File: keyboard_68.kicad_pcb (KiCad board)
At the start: 2 copper layers, 330.2 x 92.3 mm, 305 parts, among them J1 Conn_01x02_Male, J10 Conn_01x02_Female, J11 Conn_01x02_Female, J12 Conn_01x02_Female, J13 Conn_01x02_Female, J14 Conn_01x02_Female, J15 Conn_01x02_Female, J16 Conn_01x02_Female, J17 Conn_01x02_Female, J18 Conn_01x02_Female, J19 Conn_01x02_Female, J2 Conn_01x02_Female, J20 Conn_01x02_Female, J21 Conn_01x02_Female, J22 Conn_01x02_Female, J23 Conn_01x02_Female, J24 Conn_01x02_Female, J25 Conn_01x02_Female, J26 Conn_01x02_Female, J27 Conn_01x02_Female, J28 Conn_01x02_Female, J29 Conn_01x02_Female, J3 Conn_01x02_Female, J30 Conn_01x02_Female, J31 Conn_01x02_Female, J32 Conn_01x02_Female, J33 Conn_01x02_Female, J34 Conn_01x02_Female, J35 Conn_01x02_Female, J36 Conn_01x02_Female, J37 Conn_01x02_Female, J38 Conn_01x02_Female, J39 Conn_01x02_Female, J4 Conn_01x02_Female, J40 Conn_01x02_Female, J41 Conn_01x02_Female, J42 Conn_01x02_Female, J43 Conn_01x02_Female, J44 Conn_01x02_Female, J45 Conn_01x02_Female, J46 Conn_01x02_Female, J47 Conn_01x02_Female, J48 Conn_01x02_Female, J49 Conn_01x02_Female, J5 Conn_01x02_Female, J50 Conn_01x02_Female, J51 Conn_01x02_Female, J52 Conn_01x02_Female, J53 Conn_01x02_Female, J54 Conn_01x02_Female, J55 Conn_01x02_Female, J56 Conn_01x02_Female, J57 Conn_01x02_Female, J58 Conn_01x02_Female, J59 Conn_01x02_Female, J6 Conn_01x02_Female, J60 Conn_01x02_Female, J61 Conn_01x02_Female, J62 Conn_01x02_Female, J63 Conn_01x02_Female, J64 Conn_01x02_Female, J65 Conn_01x02_Female, J66 Conn_01x02_Female, J67 Conn_01x02_Female, J68 Conn_01x02_Female, J69 Conn_01x02_Female, J7 Conn_01x02_Female, J8 Conn_01x02_Female, J9 Conn_01x02_Female, Q1 DMG2305, U1 USB_C, U2 nRF52840_som, U3 MT3608

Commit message: V2
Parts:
- removed RESET: SW_Push, Button_Switch_SMD:Panasonic_EVQPUJ_EVQPUA
- added J70: Conn_02x03_Odd_Even, Connector:Tag-Connect_TC2030-IDC-NL_2x03_P1.27mm_Vertical, B.Cu at (360.2, 86.4)
- added R10: 100k, Resistor_SMD:R_0805_2012Metric, F.Cu at (346.5, 68.3)
- added R9: 100k, Resistor_SMD:R_0805_2012Metric, F.Cu at (346.5, 70.4)
- added SW1: SW_Push, Button_Switch_SMD:Panasonic_EVQPUJ_EVQPUA, F.Cu at (369.8, 87.4)
- C73, D11, D16, D26, D4, D5, D59, D6, D62, D9, FB1, FB2, L1, R2, R3, R4, R7, U3: moved to B.Cu
- U1: footprint USB_C_Receptacle_Amphenol_12401610E4-2A:USB_C_Receptacle_Amphenol_12401610E4-2A -> Connector_USB:USB_C_Receptacle_Amphenol_12401610E4-2A
- moved FB2 5.31 mm to (326.0, 38.2)
- moved FB1 4.14 mm to (327.3, 38.2)
- moved R2 3.95 mm to (322.3, 36.6), turned to 180 degrees
- moved C3 1.81 mm to (136.5, 74.3)
- moved C18 1.68 mm to (156.2, 74.3)
- moved C39 1.65 mm to (236.5, 36.4)
- moved C62 1.65 mm to (179.2, 36.4)
- moved C43 1.61 mm to (80.0, 74.3)
- moved C34 1.61 mm to (203.3, 112.4)
- moved C10 1.55 mm to (73.2, 112.4)
- moved C16 1.55 mm to (127.7, 112.4)
- moved C25 1.55 mm to (167.8, 112.4)
- moved C44 1.55 mm to (251.3, 74.3)
- moved C46 1.55 mm to (99.3, 74.3)
- moved C56 1.55 mm to (300.9, 74.3)
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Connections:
- net Net-(C2-Pad2) renamed nRST
- U2 pad 10: COLUMN_9 -> Net-(U2-Pad10)
- U2 pad 11: COLUMN_8 -> Net-(U2-Pad11)
- U2 pad 12: COLUMN_7 -> Net-(U2-Pad12)
- U2 pad 13: COLUMN_6 -> COLUMN_5
- U2 pad 14: COLUMN_5 -> Net-(U2-Pad14)
- U2 pad 17: COLUMN_2 -> Net-(U2-Pad17)
- U2 pad 18: Net-(U2-Pad18) -> COLUMN_0
- U2 pad 19: Net-(U2-Pad19) -> COLUMN_1
- U2 pad 20: COLUMN_1 -> COLUMN_2
- U2 pad 21: COLUMN_0 -> Net-(U2-Pad21)
- U2 pad 24: Net-(U2-Pad24) -> COLUMN_14
- U2 pad 26: Net-(U2-Pad26) -> ROW_2
- U2 pad 28: Net-(U2-Pad28) -> COLUMN_6
- U2 pad 3: COLUMN_15 -> Net-(U2-Pad3)
- U2 pad 34: Net-(U2-Pad34) -> COLUMN_13
- U2 pad 36: Net-(U2-Pad36) -> COLUMN_12
- U2 pad 38: Net-(U2-Pad38) -> VDIV
- U2 pad 4: COLUMN_14 -> ROW_0
- U2 pad 40: LED_DATA -> COLUMN_10
- U2 pad 42: Net-(U2-Pad42) -> LED_DATA
- U2 pad 45: Net-(U2-Pad45) -> ROW_3
- U2 pad 46: Net-(U2-Pad46) -> COLUMN_11
- U2 pad 49: Net-(U2-Pad49) -> COLUMN_7
- U2 pad 5: COLUMN_13 -> Net-(U2-Pad5)
- U2 pad 50: ROW_0 -> Net-(U2-Pad50)
- U2 pad 51: ROW_1 -> COLUMN_8
- U2 pad 52: ROW_2 -> Net-(U2-Pad52)
- U2 pad 53: ROW_3 -> COLUMN_9
- U2 pad 54: ROW_4 -> Net-(U2-Pad54)
- U2 pad 56: Net-(U2-Pad56) -> SWCLK
- U2 pad 57: Net-(U2-Pad57) -> SWDIO
- U2 pad 58: Net-(U2-Pad58) -> ROW_4
- U2 pad 6: COLUMN_12 -> ROW_1
- U2 pad 7: COLUMN_11 -> Net-(U2-Pad7)
- U2 pad 8: COLUMN_10 -> COLUMN_15
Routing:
- net COLUMN_5: track 290.3 -> 403.3 mm, vias 5 -> 7
- net GND: track 307.4 -> 217.0 mm, vias 154 -> 149
- net COLUMN_6: track 273.3 -> 348.7 mm
- net COLUMN_4: track 312.6 -> 383.1 mm, vias 3 -> 6
- net COLUMN_10: track 208.6 -> 161.8 mm
- net LED_POWER: track 95.1 -> 48.7 mm, vias 48 -> 10
- net COLUMN_12: track 136.3 -> 94.9 mm, vias 1 -> 4
- net COLUMN_11: track 187.9 -> 148.9 mm, vias 1 -> 2
- net COLUMN_14: track 63.5 -> 25.0 mm, vias 3 -> 1
- net ROW_0: track 398.3 -> 363.8 mm, vias 2 -> 0
- net ROW_2: track 328.6 -> 295.9 mm, vias 0 -> 2
- net COLUMN_13: track 91.6 -> 64.7 mm
- net ROW_1: track 365.7 -> 339.5 mm, vias 2 -> 0
- net COLUMN_9: track 231.7 -> 207.5 mm, vias 5 -> 3
- net COLUMN_8: track 244.8 -> 220.8 mm, vias 5 -> 3
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- removed copper zone on F.Cu, net Net-(C1-Pad1)
- removed copper zone on F.Cu, net VDD_BAT
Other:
- board size 330.2 x 92.3 mm -> 330 x 94 mm
- net class LED_POWER: clearance 0.2 -> 0.3; trace_width 0.6 -> 0.5
- net class VBAT added: clearance 0.3, trace_width 0.5, via_dia 0.6, via_drill 0.4
- net class VBUS: clearance 0.2 -> 0.3; trace_width 0.6 -> 0.5
- board text added: "Keyboard_68 Rev.: 2.0 (c) crohloff"

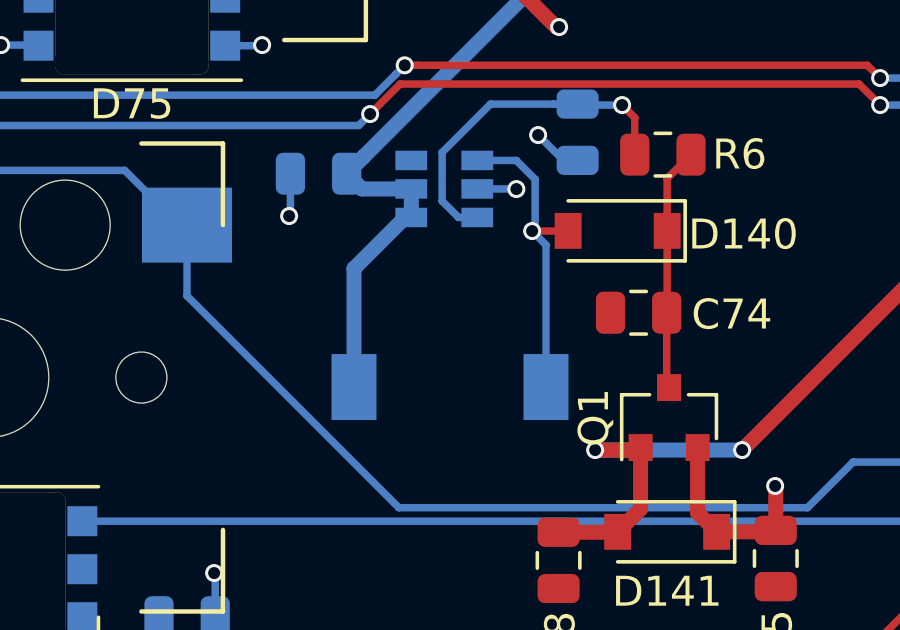
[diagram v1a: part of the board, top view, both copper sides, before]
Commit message: changed inductor and usb connector
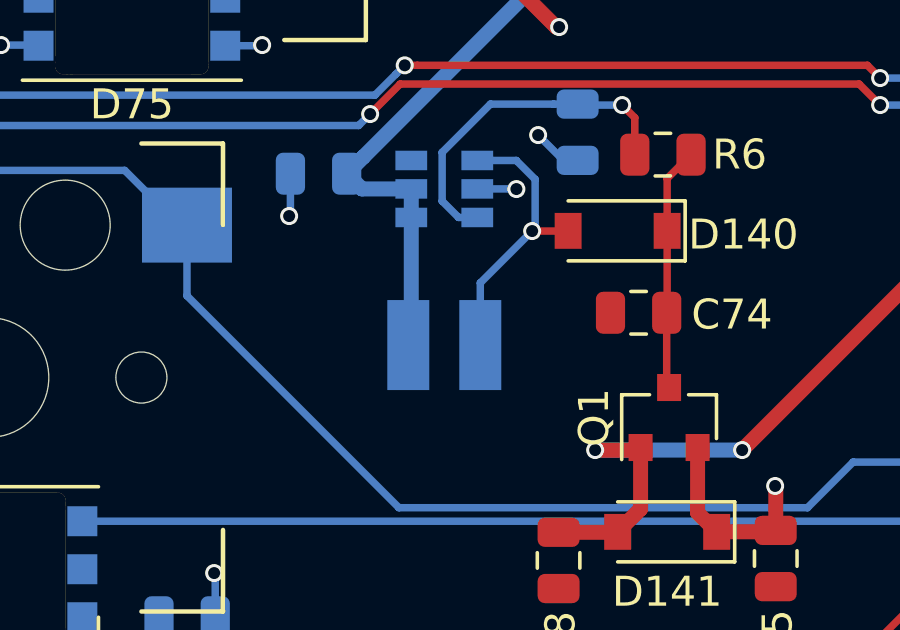
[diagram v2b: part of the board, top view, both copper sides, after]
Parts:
- L1: footprint Inductor_SMD:L_7.3x7.3_H4.5 -> L_3x3_H1.5:L_3x3_H1.5
- U1: footprint Connector_USB:USB_C_Receptacle_Amphenol_12401610E4-2A -> USB_C_Receptacle_Amphenol_12401610E4-2A:USB_C_Receptacle_Amphenol_12401610E4-2A
- moved L1 1.41 mm to (318.1, 87.5)
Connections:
- D127 pad 2: Net-(D127-Pad2) -> (no net)
- J70 pad 6: Net-(J70-Pad6) -> (no net)
- U1 pad A10: Net-(U1-PadA10) -> (no net)
- U1 pad A11: Net-(U1-PadA11) -> (no net)
- U1 pad A2: Net-(U1-PadA2) -> (no net)
- U1 pad A3: Net-(U1-PadA3) -> (no net)
- U1 pad A8: Net-(U1-PadA8) -> (no net)
- U1 pad B10: Net-(U1-PadB10) -> (no net)
- U1 pad B11: Net-(U1-PadB11) -> (no net)
- U1 pad B2: Net-(U1-PadB2) -> (no net)
- U1 pad B3: Net-(U1-PadB3) -> (no net)
- U1 pad B8: Net-(U1-PadB8) -> (no net)
- U2 pad 10: Net-(U2-Pad10) -> (no net)
- U2 pad 11: Net-(U2-Pad11) -> (no net)
- U2 pad 12: Net-(U2-Pad12) -> (no net)
- U2 pad 14: Net-(U2-Pad14) -> (no net)
- U2 pad 17: Net-(U2-Pad17) -> (no net)
- U2 pad 2: Net-(U2-Pad2) -> (no net)
- U2 pad 21: Net-(U2-Pad21) -> (no net)
- U2 pad 23: Net-(U2-Pad23) -> (no net)
- U2 pad 25: Net-(U2-Pad25) -> (no net)
- U2 pad 27: Net-(U2-Pad27) -> (no net)
- U2 pad 3: Net-(U2-Pad3) -> (no net)
- U2 pad 35: Net-(U2-Pad35) -> (no net)
- U2 pad 37: Net-(U2-Pad37) -> (no net)
- U2 pad 41: Net-(U2-Pad41) -> (no net)
- U2 pad 43: Net-(U2-Pad43) -> (no net)
- U2 pad 44: Net-(U2-Pad44) -> (no net)
- U2 pad 47: Net-(U2-Pad47) -> (no net)
- U2 pad 48: Net-(U2-Pad48) -> (no net)
- U2 pad 5: Net-(U2-Pad5) -> (no net)
- U2 pad 50: Net-(U2-Pad50) -> (no net)
- U2 pad 52: Net-(U2-Pad52) -> (no net)
- U2 pad 54: Net-(U2-Pad54) -> (no net)
- U2 pad 7: Net-(U2-Pad7) -> (no net)
- U2 pad 9: Net-(U2-Pad9) -> (no net)
- U3 pad 6: Net-(U3-Pad6) -> (no net)
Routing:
- net VDD_BAT: track 47.4 -> 45.3 mm
- net Net-(D140-Pad2): track 10.5 -> 9.67 mm

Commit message: reset switch model added
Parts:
- SW1: footprint Button_Switch_SMD:Panasonic_EVQPUJ_EVQPUA -> custom_footprints:Panasonic_EVQPUJ_EVQPUA
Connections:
- D127 pad 2: (no net) -> Net-(D127-Pad2)
- J70 pad 6: (no net) -> Net-(J70-Pad6)
- U1 pad A10: (no net) -> Net-(U1-PadA10)
- U1 pad A11: (no net) -> Net-(U1-PadA11)
- U1 pad A2: (no net) -> Net-(U1-PadA2)
- U1 pad A3: (no net) -> Net-(U1-PadA3)
- U1 pad A8: (no net) -> Net-(U1-PadA8)
- U1 pad B10: (no net) -> Net-(U1-PadB10)
- U1 pad B11: (no net) -> Net-(U1-PadB11)
- U1 pad B2: (no net) -> Net-(U1-PadB2)
- U1 pad B3: (no net) -> Net-(U1-PadB3)
- U1 pad B8: (no net) -> Net-(U1-PadB8)
- U2 pad 10: (no net) -> Net-(U2-Pad10)
- U2 pad 11: (no net) -> Net-(U2-Pad11)
- U2 pad 12: (no net) -> Net-(U2-Pad12)
- U2 pad 14: (no net) -> Net-(U2-Pad14)
- U2 pad 17: (no net) -> Net-(U2-Pad17)
- U2 pad 2: (no net) -> Net-(U2-Pad2)
- U2 pad 21: (no net) -> Net-(U2-Pad21)
- U2 pad 23: (no net) -> Net-(U2-Pad23)
- U2 pad 25: (no net) -> Net-(U2-Pad25)
- U2 pad 27: (no net) -> Net-(U2-Pad27)
- U2 pad 3: (no net) -> Net-(U2-Pad3)
- U2 pad 35: (no net) -> Net-(U2-Pad35)
- U2 pad 37: (no net) -> Net-(U2-Pad37)
- U2 pad 41: (no net) -> Net-(U2-Pad41)
- U2 pad 43: (no net) -> Net-(U2-Pad43)
- U2 pad 44: (no net) -> Net-(U2-Pad44)
- U2 pad 47: (no net) -> Net-(U2-Pad47)
- U2 pad 48: (no net) -> Net-(U2-Pad48)
- U2 pad 5: (no net) -> Net-(U2-Pad5)
- U2 pad 50: (no net) -> Net-(U2-Pad50)
- U2 pad 52: (no net) -> Net-(U2-Pad52)
- U2 pad 54: (no net) -> Net-(U2-Pad54)
- U2 pad 7: (no net) -> Net-(U2-Pad7)
- U2 pad 9: (no net) -> Net-(U2-Pad9)
- U3 pad 6: (no net) -> Net-(U3-Pad6)

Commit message: pulled usb connector out
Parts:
- moved U1 12.0 mm to (326.8, 16.4)
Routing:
- net Net-(D1-Pad2): track 26.3 -> 39.2 mm
- net Net-(R1-Pad1): track 11.2 -> 23.2 mm
- net Net-(R2-Pad1): track 12.2 -> 24.2 mm
- net Net-(C1-Pad1): track 38.1 -> 50.1 mm
- net Net-(FB1-Pad2): track 19.3 -> 31.3 mm
- net Net-(D1-Pad3): track 38.6 -> 50.3 mm
- net Net-(FB2-Pad2): track 29.2 -> 40.4 mm
- net ROW_0: track 363.8 -> 363.9 mm, vias 0 -> 2
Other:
- board size 330 x 94 mm -> 330 x 106 mm
